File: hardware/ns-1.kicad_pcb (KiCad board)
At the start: 4 copper layers, 172 x 135 mm, 74 parts, among them J1 AudioJack3, J2 AudioJack2, J3 AudioJack2, J4 AudioJack2, J5 AudioJack2, J6 Conn_01x11, J7 USB_C_Receptacle_USB2.0_16P, SW1 SW_Push_45deg, SW10 SW_Push_45deg, SW11 SW_Push_45deg, SW12 SW_Push_45deg, SW13 SW_Push_45deg, SW14 SW_Push_45deg, SW15 SW_Push_45deg, SW16 SW_Push_45deg, SW17 SW_Push_45deg, SW18 SW_Push_45deg, SW19 SW_Push_45deg, SW2 RotaryEncoder_Switch_MP, SW20 SW_Push, SW3 SW_Push_45deg, SW4 SW_Push_45deg, SW5 RotaryEncoder_Switch_MP, SW6 SW_Push_45deg, SW7 RotaryEncoder_Switch_MP, SW8 SW_Push_45deg, SW9 SW_Push_45deg, U1 Teensy4.1, U2 Teensy4.0_AudioShield_REVD

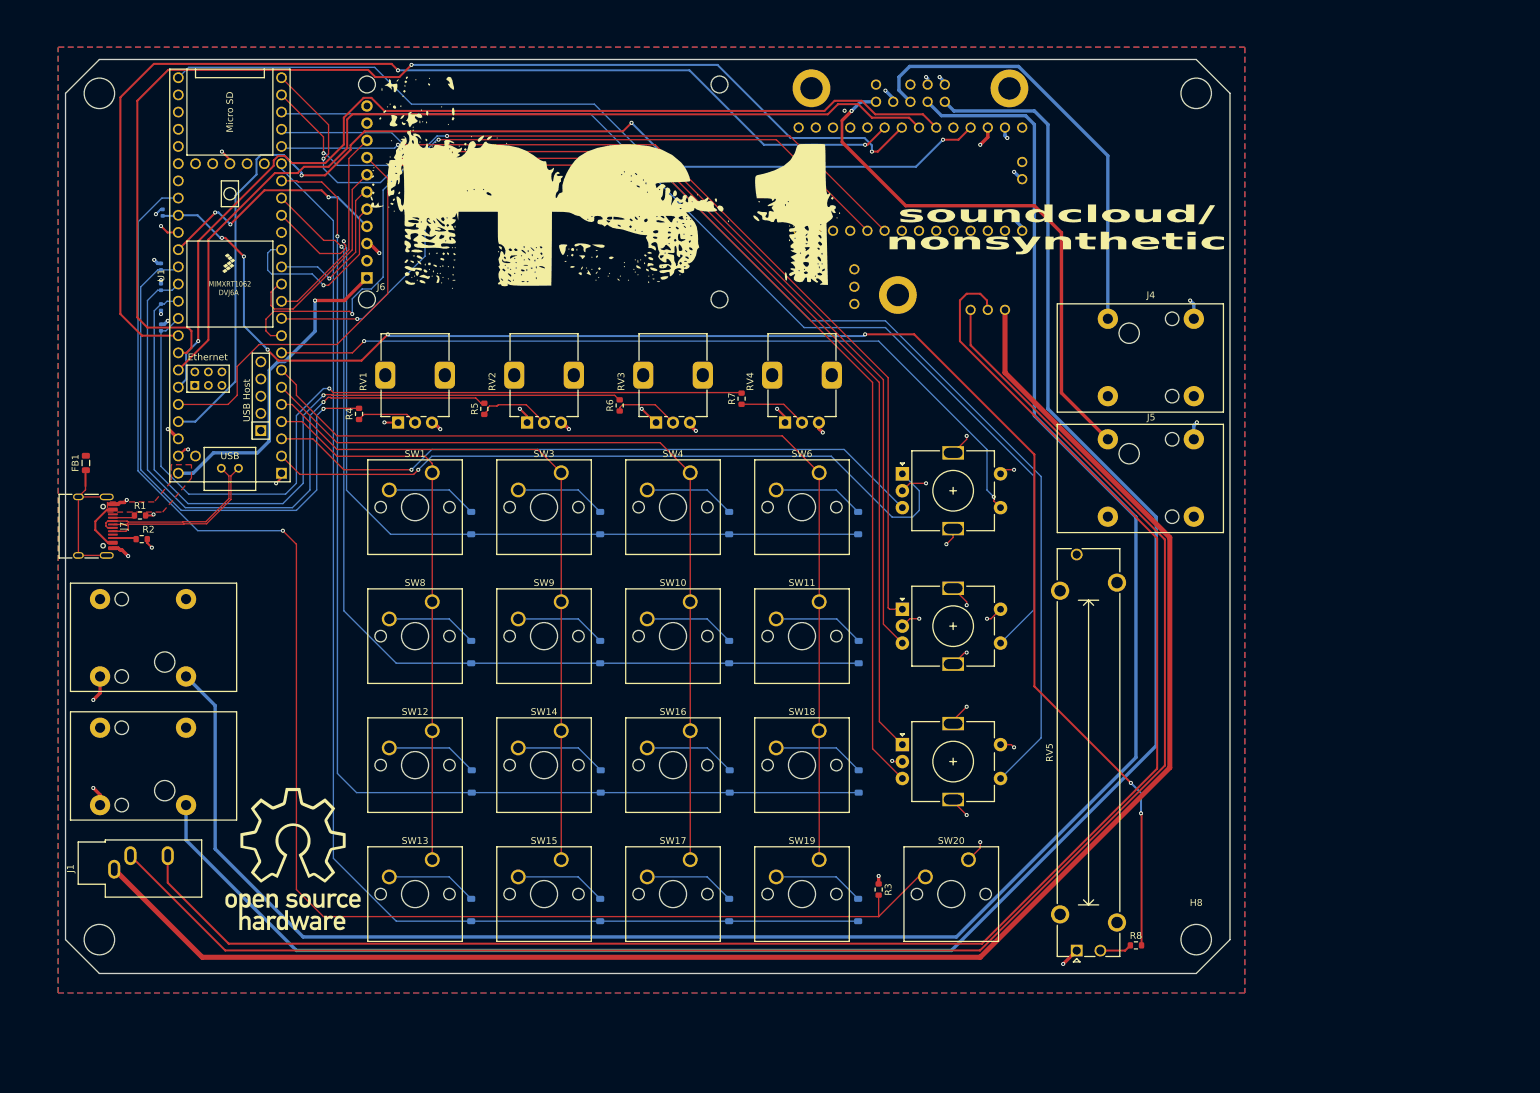
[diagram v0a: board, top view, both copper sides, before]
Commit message: start rearranging layout
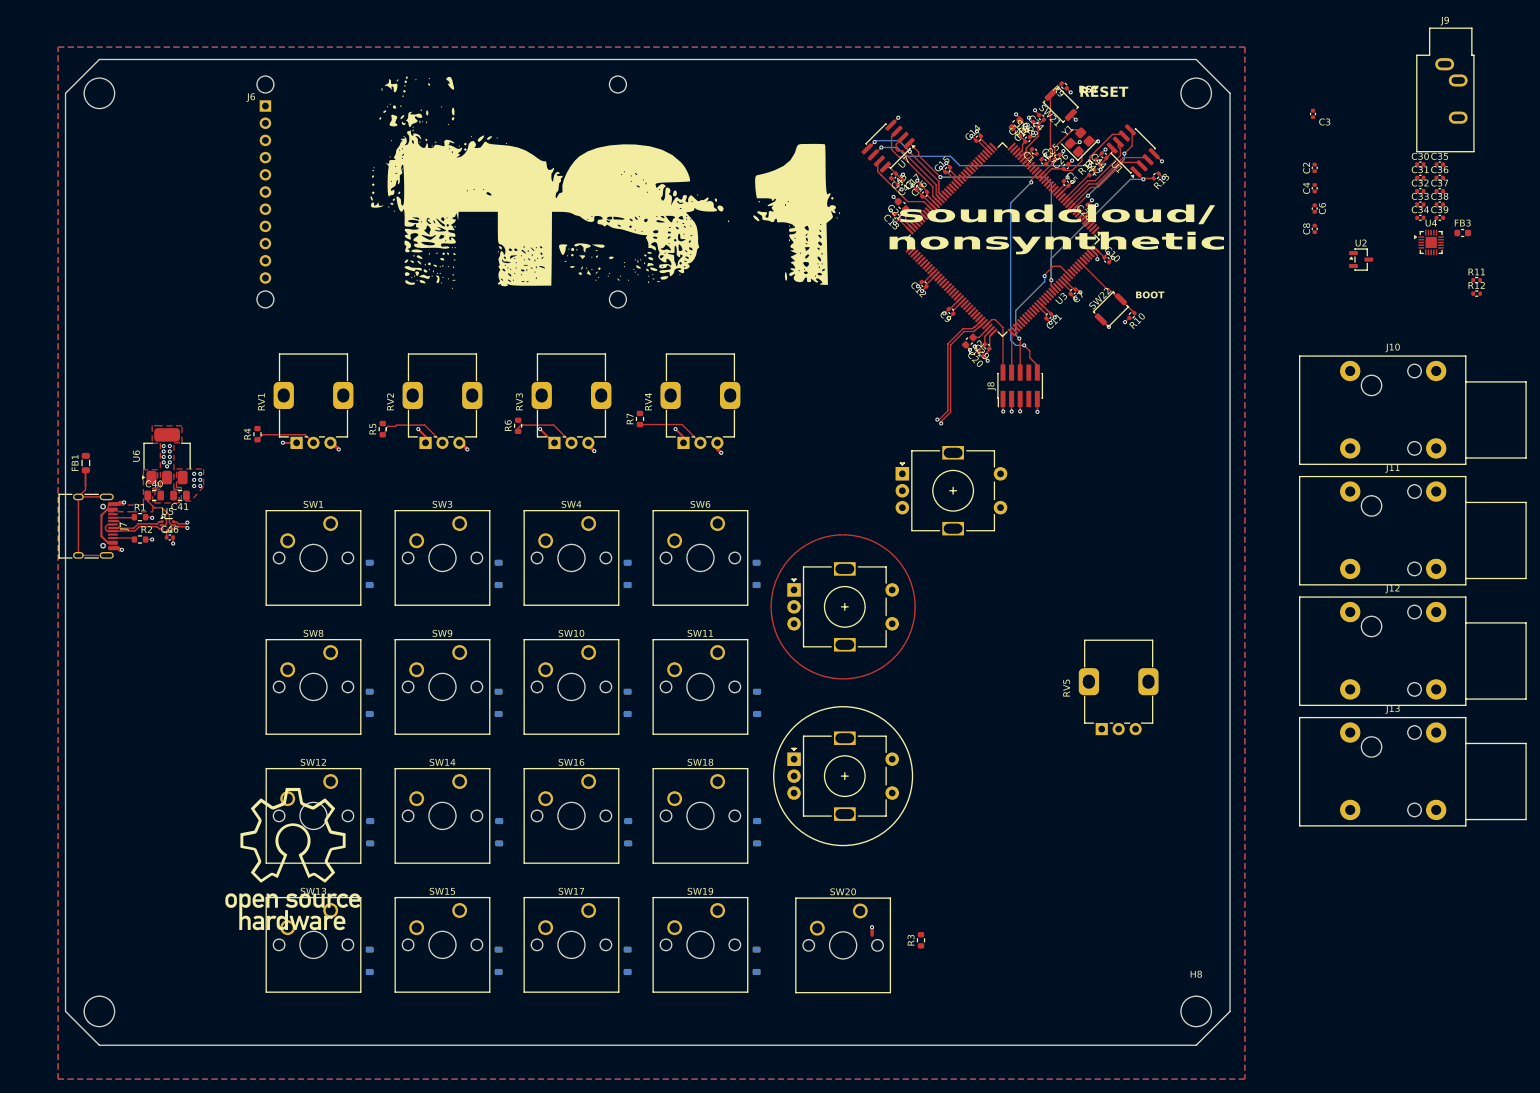
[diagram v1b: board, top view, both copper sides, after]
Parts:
- removed J1: AudioJack3, Connector_Audio:Jack_3.5mm_CUI_SJ1-3533NG_Horizontal
- removed J2, J3, J4, J5: AudioJack2, Connector_Audio:Jack_6.35mm_Neutrik_NRJ4HF_Horizontal
- removed R8: 100, Resistor_SMD:R_0603_1608Metric
- added C1: 100n, Capacitor_SMD:C_0402_1005Metric, F.Cu at (216.5, 37.3)
- added C10: 100n, Capacitor_SMD:C_0402_1005Metric, F.Cu at (227.2, 53.3)
- added C11: 100n, Capacitor_SMD:C_0402_1005Metric, F.Cu at (218.6, 61.6)
- added C12: 100n, Capacitor_SMD:C_0402_1005Metric, F.Cu at (200.2, 56.9)
- added C13: 100n, Capacitor_SMD:C_0402_1005Metric, F.Cu at (196.2, 46.9)
- added C14: 100n, Capacitor_SMD:C_0402_1005Metric, F.Cu at (208.2, 35.4)
- added C15: 100n, Capacitor_SMD:C_0402_1005Metric, F.Cu at (203.7, 40.0)
- added C16: 100n, Capacitor_SMD:C_0402_1005Metric, F.Cu at (200.3, 43.6)
- added C17: 4.7u, Capacitor_SMD:C_0402_1005Metric, F.Cu at (199.4, 42.6)
- added C18: 100n, Capacitor_SMD:C_0402_1005Metric, F.Cu at (215.5, 35.5)
- added C19: 1u, Capacitor_SMD:C_0402_1005Metric, F.Cu at (214.7, 34.6)
- added C20: 1u, Capacitor_SMD:C_0402_1005Metric, F.Cu at (208.6, 67.2)
- added C21: 2.2u, Capacitor_SMD:C_0603_1608Metric, F.Cu at (197.0, 45.3)
- added C22: 2.2u, Capacitor_SMD:C_0603_1608Metric, F.Cu at (206.9, 65.3)
- added C23: 1u, Capacitor_SMD:C_0402_1005Metric, F.Cu at (216.7, 33.3)
- added C24: 100n, Capacitor_SMD:C_0402_1005Metric, F.Cu at (217.6, 32.3)
- added C25: 15p, Capacitor_SMD:C_0402_1005Metric, F.Cu at (219.9, 38.2)
- added C26: 15p, Capacitor_SMD:C_0402_1005Metric, F.Cu at (221.2, 39.6)
- added C27: 100n, Capacitor_SMD:C_0402_1005Metric, F.Cu at (217.9, 38.8)
- added C28: 1u, Capacitor_SMD:C_0402_1005Metric, F.Cu at (224.7, 45.5)
- added C29: 100n, Capacitor_SMD:C_0402_1005Metric, F.Cu at (209.5, 66.1)
- added C30: 1u, Capacitor_SMD:C_0402_1005Metric, F.Cu at (273.5, 39.2)
- added C31: 1u, Capacitor_SMD:C_0402_1005Metric, F.Cu at (273.5, 41.2)
- added C32: 100n, Capacitor_SMD:C_0402_1005Metric, F.Cu at (273.5, 43.2)
- added C33: 100n, Capacitor_SMD:C_0402_1005Metric, F.Cu at (273.5, 45.2)
- added C34: 100n, Capacitor_SMD:C_0402_1005Metric, F.Cu at (273.5, 47.1)
- added C35: 100n, Capacitor_SMD:C_0402_1005Metric, F.Cu at (276.4, 39.2)
- added C36: 1u, Capacitor_SMD:C_0402_1005Metric, F.Cu at (276.4, 41.2)
- added C37: 1u, Capacitor_SMD:C_0402_1005Metric, F.Cu at (276.4, 43.2)
- added C38: 1u, Capacitor_SMD:C_0402_1005Metric, F.Cu at (276.4, 45.2)
- added C39: 1u, Capacitor_SMD:C_0402_1005Metric, F.Cu at (276.4, 47.1)
- added C40: 4.7u, Capacitor_SMD:C_0805_2012Metric, F.Cu at (86.5, 88.1)
- added C41: 4.7u, Capacitor_SMD:C_0805_2012Metric, F.Cu at (90.3, 88.1)
- added C42: 1u, Capacitor_SMD:C_0402_1005Metric, F.Cu at (225.9, 38.9)
- added C43: 1u, Capacitor_SMD:C_0402_1005Metric, F.Cu at (196.7, 41.9)
- added C44: 100n, Capacitor_SMD:C_0402_1005Metric, F.Cu at (226.8, 37.9)
- added C45: 100n, Capacitor_SMD:C_0402_1005Metric, F.Cu at (195.7, 40.9)
- added C46: 100n, Capacitor_SMD:C_0402_1005Metric, F.Cu at (88.8, 94.3)
- added C5: 100n, Capacitor_SMD:C_0402_1005Metric, F.Cu at (221.2, 42.0)
- added C7: 100n, Capacitor_SMD:C_0402_1005Metric, F.Cu at (222.2, 58.0)
- added C9: 100n, Capacitor_SMD:C_0402_1005Metric, F.Cu at (204.2, 60.9)
- added FB2: 120R, Inductor_SMD:L_0603_1608Metric, F.Cu at (213.8, 33.2)
- added FB3: 120R, Inductor_SMD:L_0603_1608Metric, F.Cu at (279.8, 49.4)
- added J10: AudioJack2, Connector_Audio:Jack_6.35mm_Neutrik_NRJ4HF_Horizontal, F.Cu at (263.1, 69.8)
- added J11: AudioJack2, Connector_Audio:Jack_6.35mm_Neutrik_NRJ4HF_Horizontal, F.Cu at (263.1, 87.6)
- added J12: AudioJack2, Connector_Audio:Jack_6.35mm_Neutrik_NRJ4HF_Horizontal, F.Cu at (263.1, 105.4)
- added J13: AudioJack2, Connector_Audio:Jack_6.35mm_Neutrik_NRJ4HF_Horizontal, F.Cu at (263.1, 123.2)
- added J8: Conn_ARM_JTAG_SWD_10, Connector_PinHeader_1.27mm:PinHeader_2x05_P1.27mm_Vertical_SMD, F.Cu at (214.4, 71.9)
- added J9: AudioJack3, Connector_Audio:Jack_3.5mm_CUI_SJ1-3533NG_Horizontal, F.Cu at (277.1, 24.4)
- added R10: 10k, Resistor_SMD:R_0402_1005Metric, F.Cu at (230.9, 61.5)
- added R11: 4.7k, Resistor_SMD:R_0402_1005Metric, F.Cu at (281.8, 56.3)
- added R12: 4.7k, Resistor_SMD:R_0402_1005Metric, F.Cu at (281.8, 58.3)
- added R13: 10k, Resistor_SMD:R_0402_1005Metric, F.Cu at (234.5, 40.9)
- added R14: 33R, Resistor_SMD:R_0402_1005Metric, F.Cu at (225.0, 40.4)
- added R9: 10k, Resistor_SMD:R_0402_1005Metric, F.Cu at (220.9, 27.6)
- added SW21: SW_Push, Button_Switch_SMD:SW_Push_SPST_NO_Alps_SKRK, F.Cu at (220.4, 30.4)
- added SW22: SW_Push, Button_Switch_SMD:SW_Push_SPST_NO_Alps_SKRK, F.Cu at (227.8, 60.6)
- added U3: STM32H723ZGTx, Package_QFP:LQFP-144_20x20mm_P0.5mm, F.Cu at (211.8, 50.3)
- added U4: SGTL5000XNLA3, Package_DFN_QFN:QFN-20-1EP_3x3mm_P0.4mm_EP1.65x1.65mm, F.Cu at (275.1, 50.8)
- added U5: USBLC6-2P6, Package_TO_SOT_SMD:SOT-666, F.Cu at (88.5, 92.5)
- added U6: AP7361C-33E, Package_TO_SOT_SMD:SOT-223-3_TabPin2, F.Cu at (88.4, 82.3)
- added U7: APS6404L-3SQRx-SN, Package_SO:SOIC-8_3.9x4.9mm_P1.27mm, F.Cu at (194.9, 36.5)
- added Y1: 25MHz, Crystal:Crystal_SMD_3225-4Pin_3.2x2.5mm, F.Cu at (223.2, 36.0)
- C2, C3, C4, C6, C8: moved to F.Cu
- RV5: footprint Potentiometer_THT:Potentiometer_Bourns_PTA4543_Single_Slide -> Potentiometer_THT:Potentiometer_Alps_RK09K_Single_Vertical
- SW1, SW10, SW11, SW12, SW13, SW14, SW15, SW16, SW17, SW18, SW19, SW20, SW3, SW4, SW6, SW8, SW9: footprint switches:SW_Cherry_MX_1.00u_PCB -> Button_Switch_Keyboard:SW_Cherry_MX_1.00u_PCB
- U1: value Teensy4.1 -> APS6404L-3SQRx-SN; footprint footprints:Teensy41 -> Package_SO:SOIC-8_3.9x4.9mm_P1.27mm
- U2: value Teensy4.0_AudioShield_REVD -> XC6206P182MR; footprint footprints:4.0audioshield -> Package_TO_SOT_SMD:SOT-23-3; moved to F.Cu
- moved C2 171.0 mm to (257.9, 39.8)
- moved C4 171.0 mm to (257.9, 42.8)
- moved C6 171.0 mm to (257.9, 45.8)
- moved C8 171.0 mm to (257.9, 48.8)
- moved C3 170.5 mm to (257.7, 31.8)
- moved U1 134.7 mm to (231.1, 37.2), turned to 135 degrees
- moved U2 50.2 mm to (264.8, 53.3), turned to 0 degrees
- moved RV5 32.9 mm to (226.4, 122.6)
- moved J6 29.5 mm to (102.9, 30.6), turned to 0 degrees
- moved SW20 17.7 mm to (190.8, 149.5)
- moved D1 16.8 mm to (118.3, 99.7)
- moved D10 16.8 mm to (118.3, 156.9)
- moved D11 16.8 mm to (137.4, 137.9)
- moved D12 16.8 mm to (137.4, 156.9)
- moved D13 16.8 mm to (156.5, 137.9)
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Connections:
- C2 pad 1: /POT1 -> /Peripherals/POT1
- C3 pad 1: /SL1 -> /Peripherals/VSK
- C4 pad 1: /POT2 -> /Peripherals/POT2
- C6 pad 1: /POT3 -> /Peripherals/POT3
- C8 pad 1: /POT4 -> /Peripherals/POT4
- D1 pad 1: Row 0 -> /Peripherals/ROW0
- D10 pad 1: Row 3 -> /Peripherals/ROW3
- D11 pad 1: Row 2 -> /Peripherals/ROW2
- D12 pad 1: Row 3 -> /Peripherals/ROW3
- D13 pad 1: Row 2 -> /Peripherals/ROW2
- D14 pad 1: Row 3 -> /Peripherals/ROW3
- D15 pad 1: Row 2 -> /Peripherals/ROW2
- D16 pad 1: Row 3 -> /Peripherals/ROW3
- D2 pad 1: Row 0 -> /Peripherals/ROW0
- D3 pad 1: Row 0 -> /Peripherals/ROW0
- D4 pad 1: Row 0 -> /Peripherals/ROW0
- D5 pad 1: Row 1 -> /Peripherals/ROW1
- D6 pad 1: Row 1 -> /Peripherals/ROW1
- D7 pad 1: Row 1 -> /Peripherals/ROW1
- D8 pad 1: Row 1 -> /Peripherals/ROW1
- D9 pad 1: Row 2 -> /Peripherals/ROW2
- J6 pad 1: +5V -> VBUS
- J6 pad 4: /SCK -> /Peripherals/SCK
- J6 pad 5: /MISO -> /Peripherals/MISO
- J6 pad 6: /MOSI -> /Peripherals/MOSI
- J6 pad 7: /TCS -> /Peripherals/TCS
- J6 pad 8: /RST -> /Peripherals/RST
- J6 pad 9: /DC -> /Peripherals/DC
- J7 pad A4: +5V -> VBUS
- J7 pad A6: /D+ -> /Power/UNPROT_D+
- J7 pad A7: /D- -> /Power/UNPROT_D-
- J7 pad A9: +5V -> VBUS
- J7 pad B4: +5V -> VBUS
- J7 pad B6: /D+ -> /Power/UNPROT_D+
- J7 pad B7: /D- -> /Power/UNPROT_D-
- J7 pad B9: +5V -> VBUS
- R3 pad 2: /BTN1 -> /Peripherals/BTN1
- R4 pad 2: /POT1 -> /Peripherals/POT1
- R5 pad 2: /POT2 -> /Peripherals/POT2
- R6 pad 2: /POT3 -> /Peripherals/POT3
- R7 pad 2: /POT4 -> /Peripherals/POT4
- SW1 pad 1: Col 0 -> /Peripherals/COL0
- SW10 pad 1: Col 2 -> /Peripherals/COL2
- SW11 pad 1: Col 3 -> /Peripherals/COL3
- SW12 pad 1: Col 0 -> /Peripherals/COL0
- SW13 pad 1: Col 0 -> /Peripherals/COL0
- SW14 pad 1: Col 1 -> /Peripherals/COL1
- SW15 pad 1: Col 1 -> /Peripherals/COL1
- SW16 pad 1: Col 2 -> /Peripherals/COL2
- SW17 pad 1: Col 2 -> /Peripherals/COL2
- SW18 pad 1: Col 3 -> /Peripherals/COL3
- SW19 pad 1: Col 3 -> /Peripherals/COL3
- SW2 pad A: /A1 -> /Peripherals/A1
- SW2 pad B: /B1 -> /Peripherals/B1
- SW2 pad S1: /S1 -> /Peripherals/S1
- SW20 pad 2: /BTN1 -> /Peripherals/BTN1
- SW3 pad 1: Col 1 -> /Peripherals/COL1
- SW4 pad 1: Col 2 -> /Peripherals/COL2
- SW5 pad A: /A2 -> /Peripherals/A2
- SW5 pad B: /B2 -> /Peripherals/B2
- SW5 pad S1: /S2 -> /Peripherals/S2
- SW6 pad 1: Col 3 -> /Peripherals/COL3
- SW7 pad A: /A3 -> /Peripherals/A3
- SW7 pad B: /B3 -> /Peripherals/B3
- SW7 pad S1: /S3 -> /Peripherals/S3
- SW8 pad 1: Col 0 -> /Peripherals/COL0
- SW9 pad 1: Col 1 -> /Peripherals/COL1
- U1 pad 1: GND -> /PSRAM/CE
- U1 pad 2: /A1 -> /PSRAM/SIO1
- U1 pad 3: /B1 -> /PSRAM/SIO2
- U1 pad 4: Col 0 -> GND
- U1 pad 5: Col 1 -> /PSRAM/SIO0
- U1 pad 6: Col 2 -> /PSRAM/SCLK
- U1 pad 7: Col 3 -> /PSRAM/SIO3
- U1 pad 8: /S1 -> +3.3V
- U2 pad 2: unconnected-(U2-0_RX1_CRX2_CS1-Pad2) -> +1V8
- U2 pad 3: unconnected-(U2-1_TX1_CTX2_MISO1-Pad3) -> +3.3V
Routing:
- net Net-(U2-LINE_IN_R): track 296.5 -> 0.00 mm
- net Net-(U2-LINE_IN_L): track 282.7 -> 0.00 mm
- net Net-(U2-HEADPHONES_R): track 252.0 -> 0.00 mm
- net Net-(U2-HEADPHONES_VGND): track 250.6 -> 0.00 mm
- net Net-(U2-HEADPHONES_L): track 249.1 -> 0.00 mm
- net /SL1: track 231.9 -> 0.00 mm, vias 7 -> 0
- net /BTN1: track 223.3 -> 0.00 mm, vias 1 -> 0
- net /S3: track 200.2 -> 0.00 mm
- net Row 3: track 187.1 -> 0.00 mm
- net /B3: track 173.5 -> 0.00 mm, vias 2 -> 0
- net Row 2: track 172.5 -> 0.00 mm, vias 1 -> 0
- net /SDA: track 168.9 -> 0.00 mm, vias 2 -> 0
- net /A3: track 163.1 -> 0.00 mm, vias 2 -> 0
- net /SCL: track 162.8 -> 0.00 mm, vias 2 -> 0
- net /MCLK: track 160.9 -> 0.00 mm, vias 3 -> 0
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- added copper zone on F.Cu, net +3.3V
- added copper zone on F.Cu, net VBUS
- removed copper zone on F.Cu, net +5V
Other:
- board size 172 x 135 mm -> 172 x 145.6 mm
- board text added: "BOOT"
- board text added: "RESET"
- board text added: "RST"

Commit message: finish placement, add sd, codec routing
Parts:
- added C47: 100n, Capacitor_SMD:C_0402_1005Metric, F.Cu at (223.8, 73.4)
- added C48: 10u, Capacitor_SMD:C_0603_1608Metric, F.Cu at (222.1, 73.9)
- added J1: Micro_SD_Card_Det2, Connector_Card:microSD_HC_Hirose_DM3AT-SF-PEJM5, F.Cu at (234.5, 72.3)
- added R15: 10k, Resistor_SMD:R_0402_1005Metric, F.Cu at (238.9, 81.0)
- added R16: 47k, Resistor_SMD:R_0402_1005Metric, F.Cu at (223.7, 80.0)
- added R17: 47k, Resistor_SMD:R_0402_1005Metric, F.Cu at (221.1, 76.8)
- added R18: 47k, Resistor_SMD:R_0402_1005Metric, F.Cu at (220.3, 73.4)
- added R19: 47k, Resistor_SMD:R_0402_1005Metric, F.Cu at (218.9, 73.4)
- added R20: 47k, Resistor_SMD:R_0402_1005Metric, F.Cu at (223.8, 67.3)
- added R21: 33R, Resistor_SMD:R_0402_1005Metric, F.Cu at (216.9, 64.6)
- added R8: 100, Resistor_SMD:R_0603_1608Metric, F.Cu at (221.2, 122.3)
- moved J9 237.5 mm to (76.0, 150.7), turned to 90 degrees
- moved FB3 196.4 mm to (83.5, 42.7), turned to 180 degrees
- moved C35 192.7 mm to (83.8, 45.8)
- moved C36 190.1 mm to (86.4, 49.1), turned to -90 degrees
- moved C33 189.7 mm to (83.8, 44.4), turned to 180 degrees
- moved C30 189.1 mm to (84.5, 34.4)
- moved C37 188.9 mm to (87.5, 49.1), turned to -90 degrees
- moved C38 187.7 mm to (88.7, 49.1), turned to 90 degrees
- moved U4 187.0 mm to (88.2, 45.0)
- moved C31 186.6 mm to (86.9, 38.3)
- moved C39 186.5 mm to (89.8, 49.1), turned to 90 degrees
- moved C34 186.2 mm to (87.4, 40.8), turned to 90 degrees
- moved C32 181.6 mm to (91.9, 45.4)
- moved U2 181.5 mm to (84.0, 37.2), turned to 90 degrees
- moved J12 172.3 mm to (91.8, 123.1), turned to 180 degrees
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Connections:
- U3 pad 111: unconnected-(U3-PC10-Pad111) -> /STM32H7/DAT2
- U3 pad 112: unconnected-(U3-PC11-Pad112) -> /STM32H7/DAT3
- U3 pad 113: unconnected-(U3-PC12-Pad113) -> Net-(U3-PC12)
- U3 pad 116: /Peripherals/S3 -> /STM32H7/CMD
- U3 pad 85: unconnected-(U3-PD14-Pad85) -> /Peripherals/S3
- U3 pad 87: unconnected-(U3-PG2-Pad87) -> /STM32H7/DET_A
- U3 pad 98: unconnected-(U3-PC8-Pad98) -> /STM32H7/DAT0
- U3 pad 99: unconnected-(U3-PC9-Pad99) -> /STM32H7/DAT1
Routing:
- net Net-(C36-Pad2): track 0.00 -> 168.0 mm, vias 0 -> 1
- net Net-(C37-Pad2): track 0.00 -> 156.9 mm, vias 0 -> 1
- net Net-(U4-HP_R): track 0.00 -> 113.9 mm, vias 0 -> 1
- net Net-(U4-HP_L): track 0.00 -> 113.4 mm, vias 0 -> 2
- net Net-(U4-HP_VGND): track 0.00 -> 113.3 mm, vias 0 -> 1
- net Net-(C39-Pad1): track 0.00 -> 97.5 mm
- net Net-(C38-Pad1): track 0.00 -> 79.7 mm
- net /STM32H7/DET_A: track 0.00 -> 58.4 mm, vias 0 -> 2
- net /STM32H7/DAT1: track 0.00 -> 39.7 mm, vias 0 -> 2
- net /STM32H7/DAT0: track 0.00 -> 38.8 mm, vias 0 -> 2
- net GND: track 80.8 -> 108.5 mm, vias 51 -> 67
- net /STM32H7/DAT3: track 0.00 -> 21.4 mm, vias 0 -> 2
- net /STM32H7/CMD: track 0.00 -> 20.2 mm, vias 0 -> 2
- net /STM32H7/DAT2: track 0.00 -> 17.2 mm
- net +3.3V: track 66.4 -> 81.4 mm, vias 31 -> 39
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
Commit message: clean up bottom layer routing & route i2s
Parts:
- moved C3 51.4 mm to (206.3, 33.2), turned to -135 degrees
- moved R12 50.9 mm to (231.2, 53.8), turned to -45 degrees
- moved C8 50.4 mm to (209.8, 33.8), turned to -135 degrees
- moved C6 48.5 mm to (211.5, 31.7), turned to 45 degrees
- moved R11 48.0 mm to (233.9, 57.3), turned to 135 degrees
- moved C4 46.7 mm to (212.3, 32.5), turned to 45 degrees
- moved C2 40.5 mm to (217.6, 36.3), turned to 135 degrees
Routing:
- net /SGTL5000/SDA: track 0.00 -> 208.5 mm, vias 0 -> 2
- net /SGTL5000/SCL: track 0.00 -> 204.3 mm
- net /SGTL5000/I2S_DOUT: track 0.00 -> 188.3 mm, vias 0 -> 2
- net /SGTL5000/I2S_DIN: track 0.00 -> 187.7 mm, vias 0 -> 2
- net /SGTL5000/I2S_SCLK: track 0.00 -> 185.7 mm, vias 0 -> 2
- net /SGTL5000/I2S_LRCLK: track 0.00 -> 184.8 mm, vias 0 -> 2
- net /SGTL5000/SYS_MCLK: track 0.00 -> 182.1 mm, vias 0 -> 2
- net Net-(C37-Pad2): track 156.9 -> 330.1 mm
- net Net-(C36-Pad2): track 168.0 -> 312.0 mm
- net /Peripherals/DC: track 0.00 -> 115.7 mm
- net /Peripherals/RST: track 0.00 -> 115.3 mm
- net /Peripherals/TCS: track 0.00 -> 114.9 mm
- net /Peripherals/MOSI: track 0.00 -> 114.5 mm
- net /Peripherals/MISO: track 0.00 -> 114.2 mm
- net /Peripherals/SCK: track 0.00 -> 113.8 mm
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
